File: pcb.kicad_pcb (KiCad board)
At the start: 2 copper layers, 48 parts, among them J1 USB_B_Mini, J2 Conn_ARM_JTAG_SWD_20, J3 Micro_SD_Card_Det1, J4 Conn_02x25_Odd_Even, J5 Conn_02x25_Odd_Even, SW1 SW_RESET, U1 STM32H750VBTx, U2 USBLC6-2P6, U3 TLV1117-33, Y2 25MHz 9uF

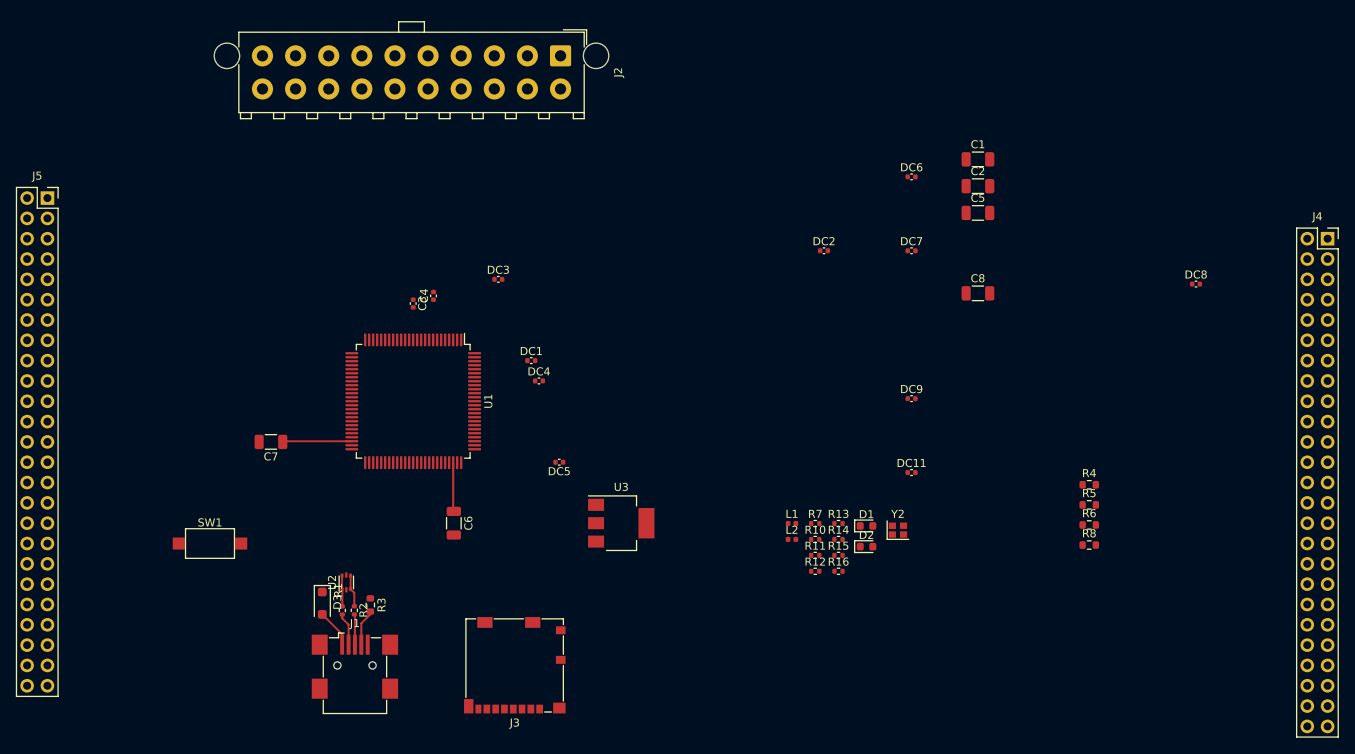
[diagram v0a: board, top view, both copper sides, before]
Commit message: ROUTE: Routing finished, still needs to be re-worked but functionality is in place
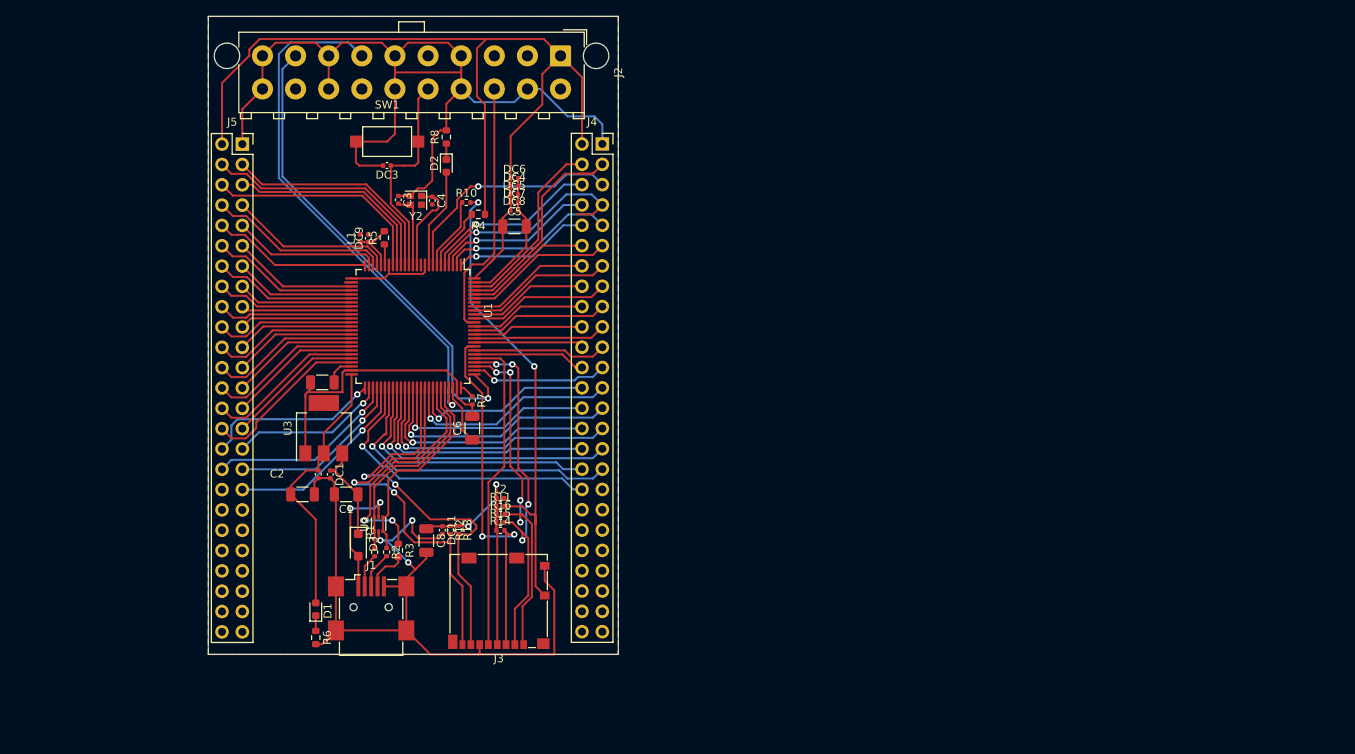
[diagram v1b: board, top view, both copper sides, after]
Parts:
- moved R6 97.7 mm to (74.2, 115.9), turned to -90 degrees
- moved R8 95.2 mm to (90.5, 53.3), turned to 90 degrees
- moved R5 94.2 mm to (82.8, 65.9), turned to 90 degrees
- moved C2 92.8 mm to (72.5, 98.0)
- moved J4 91.4 mm to (110.0, 54.2)
- moved C1 89.4 mm to (78.0, 98.0), turned to 180 degrees
- moved DC8 85.7 mm to (99.0, 62.5)
- moved R4 83.5 mm to (94.5, 63.0), turned to 180 degrees
- moved C8 75.6 mm to (88.0, 103.8), turned to -90 degrees
- moved Y2 73.0 mm to (86.7, 61.2), turned to 180 degrees
- moved D2 70.9 mm to (90.5, 56.9), turned to -90 degrees
- moved DC9 70.8 mm to (80.8, 66.0), turned to 90 degrees
- moved D1 69.6 mm to (74.2, 112.4), turned to 90 degrees
- moved DC2 69.1 mm to (74.5, 95.5), turned to -90 degrees
- moved L1 64.7 mm to (79.8, 66.0), turned to 90 degrees
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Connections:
- J4 pad 1: unconnected-(J4-Pin_1-Pad1) -> Earth
- J4 pad 10: unconnected-(J4-Pin_10-Pad10) -> PE2
- J4 pad 11: unconnected-(J4-Pin_11-Pad11) -> PB8
- J4 pad 12: unconnected-(J4-Pin_12-Pad12) -> PB9
- J4 pad 13: unconnected-(J4-Pin_13-Pad13) -> PB6
- J4 pad 14: unconnected-(J4-Pin_14-Pad14) -> PB7
- J4 pad 15: unconnected-(J4-Pin_15-Pad15) -> PB4
- J4 pad 16: unconnected-(J4-Pin_16-Pad16) -> PB5
- J4 pad 17: unconnected-(J4-Pin_17-Pad17) -> PD6
- J4 pad 18: unconnected-(J4-Pin_18-Pad18) -> PD7
- J4 pad 19: unconnected-(J4-Pin_19-Pad19) -> PD4
- J4 pad 2: unconnected-(J4-Pin_2-Pad2) -> BOOT0
- J4 pad 20: unconnected-(J4-Pin_20-Pad20) -> PD5
- J4 pad 21: unconnected-(J4-Pin_21-Pad21) -> PD1
- J4 pad 22: unconnected-(J4-Pin_22-Pad22) -> PD3
- J4 pad 23: unconnected-(J4-Pin_23-Pad23) -> PA15
- J4 pad 24: unconnected-(J4-Pin_24-Pad24) -> PD0
- J4 pad 25: unconnected-(J4-Pin_25-Pad25) -> PA8
- J4 pad 26: unconnected-(J4-Pin_26-Pad26) -> PA9
- J4 pad 27: unconnected-(J4-Pin_27-Pad27) -> PC6
- J4 pad 28: unconnected-(J4-Pin_28-Pad28) -> PC7
- J4 pad 29: unconnected-(J4-Pin_29-Pad29) -> PD14
- J4 pad 3: unconnected-(J4-Pin_3-Pad3) -> PE0
- J4 pad 30: unconnected-(J4-Pin_30-Pad30) -> PD15
- J4 pad 31: unconnected-(J4-Pin_31-Pad31) -> PD12
- J4 pad 32: unconnected-(J4-Pin_32-Pad32) -> PD13
- J4 pad 33: unconnected-(J4-Pin_33-Pad33) -> PD10
- J4 pad 34: unconnected-(J4-Pin_34-Pad34) -> PD11
- J4 pad 36: unconnected-(J4-Pin_36-Pad36) -> PD9
- J4 pad 4: unconnected-(J4-Pin_4-Pad4) -> PE1
- J4 pad 5: unconnected-(J4-Pin_5-Pad5) -> PC14
- J4 pad 6: unconnected-(J4-Pin_6-Pad6) -> PE6
- J4 pad 7: unconnected-(J4-Pin_7-Pad7) -> PE5
- J4 pad 8: unconnected-(J4-Pin_8-Pad8) -> PE4
- J4 pad 9: unconnected-(J4-Pin_9-Pad9) -> PE3
- J5 pad 1: PE0 -> Earth
- J5 pad 10: PE9 -> PA3
- J5 pad 11: PE10 -> PA4
- J5 pad 12: PE11 -> PA5
- J5 pad 13: PE12 -> PA6
- J5 pad 14: PE13 -> PA7
- J5 pad 15: PE14 -> PC4
- J5 pad 16: PE15 -> PC5
- J5 pad 17: unconnected-(J5-Pin_17-Pad17) -> PB0
- J5 pad 18: unconnected-(J5-Pin_18-Pad18) -> PB1
- J5 pad 19: unconnected-(J5-Pin_19-Pad19) -> PB2
- J5 pad 2: PE1 -> BOOT0
- J5 pad 20: unconnected-(J5-Pin_20-Pad20) -> PE7
- J5 pad 21: unconnected-(J5-Pin_21-Pad21) -> PE8
- J5 pad 22: unconnected-(J5-Pin_22-Pad22) -> PE9
- J5 pad 23: unconnected-(J5-Pin_23-Pad23) -> PE10
- J5 pad 24: unconnected-(J5-Pin_24-Pad24) -> PE11
- J5 pad 25: unconnected-(J5-Pin_25-Pad25) -> PE12
- J5 pad 26: unconnected-(J5-Pin_26-Pad26) -> PE13
- J5 pad 27: unconnected-(J5-Pin_27-Pad27) -> PE14
- J5 pad 28: unconnected-(J5-Pin_28-Pad28) -> PE15
- J5 pad 29: unconnected-(J5-Pin_29-Pad29) -> PB10
- J5 pad 3: PE2 -> PC0
- J5 pad 30: unconnected-(J5-Pin_30-Pad30) -> PB11
- J5 pad 31: unconnected-(J5-Pin_31-Pad31) -> PB13
- J5 pad 32: unconnected-(J5-Pin_32-Pad32) -> PB12
- J5 pad 33: unconnected-(J5-Pin_33-Pad33) -> PB15
- J5 pad 34: unconnected-(J5-Pin_34-Pad34) -> PB14
- J5 pad 35: unconnected-(J5-Pin_35-Pad35) -> PD8
- J5 pad 4: PE3 -> PC1
- J5 pad 5: PE4 -> PC2
- J5 pad 6: PE5 -> PC3
- J5 pad 7: PE6 -> PA0
- J5 pad 8: PE7 -> PA1
- J5 pad 9: PE8 -> PA2
- U1 pad 15: unconnected-(U1-PC0-Pad15) -> PC0
- U1 pad 16: unconnected-(U1-PC1-Pad16) -> PC1
- U1 pad 17: unconnected-(U1-PC2_C-Pad17) -> PC2
- U1 pad 18: unconnected-(U1-PC3_C-Pad18) -> PC3
- U1 pad 22: unconnected-(U1-PA0-Pad22) -> PA0
- U1 pad 23: unconnected-(U1-PA1-Pad23) -> PA1
- U1 pad 24: unconnected-(U1-PA2-Pad24) -> PA2
- U1 pad 25: unconnected-(U1-PA3-Pad25) -> PA3
- U1 pad 28: unconnected-(U1-PA4-Pad28) -> PA4
- U1 pad 29: unconnected-(U1-PA5-Pad29) -> PA5
- U1 pad 30: unconnected-(U1-PA6-Pad30) -> PA6
- U1 pad 31: unconnected-(U1-PA7-Pad31) -> PA7
- U1 pad 32: unconnected-(U1-PC4-Pad32) -> PC4
- U1 pad 33: unconnected-(U1-PC5-Pad33) -> PC5
- U1 pad 34: unconnected-(U1-PB0-Pad34) -> PB0
- U1 pad 35: unconnected-(U1-PB1-Pad35) -> PB1
- U1 pad 36: unconnected-(U1-PB2-Pad36) -> PB2
- U1 pad 46: unconnected-(U1-PB10-Pad46) -> PB10
- U1 pad 47: unconnected-(U1-PB11-Pad47) -> PB11
- U1 pad 51: unconnected-(U1-PB12-Pad51) -> PB12
- U1 pad 52: unconnected-(U1-PB13-Pad52) -> PB13
- U1 pad 53: unconnected-(U1-PB14-Pad53) -> PB14
- U1 pad 54: unconnected-(U1-PB15-Pad54) -> PB15
- U1 pad 55: unconnected-(U1-PD8-Pad55) -> PD8
- U1 pad 56: unconnected-(U1-PD9-Pad56) -> PD9
- U1 pad 57: unconnected-(U1-PD10-Pad57) -> PD10
- U1 pad 58: unconnected-(U1-PD11-Pad58) -> PD11
- U1 pad 59: unconnected-(U1-PD12-Pad59) -> PD12
- U1 pad 60: unconnected-(U1-PD13-Pad60) -> PD13
- U1 pad 61: unconnected-(U1-PD14-Pad61) -> PD14
- U1 pad 62: unconnected-(U1-PD15-Pad62) -> PD15
- U1 pad 63: unconnected-(U1-PC6-Pad63) -> PC6
- U1 pad 64: unconnected-(U1-PC7-Pad64) -> PC7
- U1 pad 67: unconnected-(U1-PA8-Pad67) -> PA8
- U1 pad 68: unconnected-(U1-PA9-Pad68) -> PA9
- U1 pad 77: unconnected-(U1-PA15-Pad77) -> PA15
- U1 pad 8: unconnected-(U1-PC14-Pad8) -> PC14
- U1 pad 81: unconnected-(U1-PD0-Pad81) -> PD0
- U1 pad 82: unconnected-(U1-PD1-Pad82) -> PD1
- U1 pad 84: unconnected-(U1-PD3-Pad84) -> PD3
- U1 pad 85: unconnected-(U1-PD4-Pad85) -> PD4
- U1 pad 86: unconnected-(U1-PD5-Pad86) -> PD5
- U1 pad 87: unconnected-(U1-PD6-Pad87) -> PD6
- U1 pad 88: unconnected-(U1-PD7-Pad88) -> PD7
- U1 pad 90: unconnected-(U1-PB4-Pad90) -> PB4
- U1 pad 91: unconnected-(U1-PB5-Pad91) -> PB5
- U1 pad 92: unconnected-(U1-PB6-Pad92) -> PB6
- U1 pad 93: unconnected-(U1-PB7-Pad93) -> PB7
- U1 pad 95: unconnected-(U1-PB8-Pad95) -> PB8
- U1 pad 96: unconnected-(U1-PB9-Pad96) -> PB9
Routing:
- net Earth: track 0.00 -> 285.5 mm, vias 0 -> 3
- net BOOT0: track 0.00 -> 158.9 mm
- net PA13: track 0.00 -> 67.4 mm, vias 0 -> 1
- net Net-(J3-DET): track 0.00 -> 60.4 mm, vias 0 -> 2
- net PA14: track 0.00 -> 60.0 mm, vias 0 -> 1
- net Net-(J3-DAT0): track 0.00 -> 50.1 mm, vias 0 -> 2
- net Net-(J3-DAT1): track 0.00 -> 49.9 mm, vias 0 -> 2
- net Net-(J3-DAT3/CD): track 0.00 -> 47.1 mm, vias 0 -> 4
- net PD2: track 0.00 -> 45.5 mm, vias 0 -> 2
- net Net-(J3-DAT2): track 0.00 -> 44.8 mm, vias 0 -> 4
- net Net-(J3-CLK): track 0.00 -> 40.1 mm
- net PD10: track 0.00 -> 39.2 mm, vias 0 -> 1
- net PD9: track 0.00 -> 38.2 mm, vias 0 -> 1
- net Net-(J3-VDD): track 0.00 -> 36.8 mm, vias 0 -> 2
- net PD12: track 0.00 -> 35.3 mm, vias 0 -> 1
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- added copper zone on F.Cu, net Earth
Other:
- board outline added: 51.2 x 79.8 mm

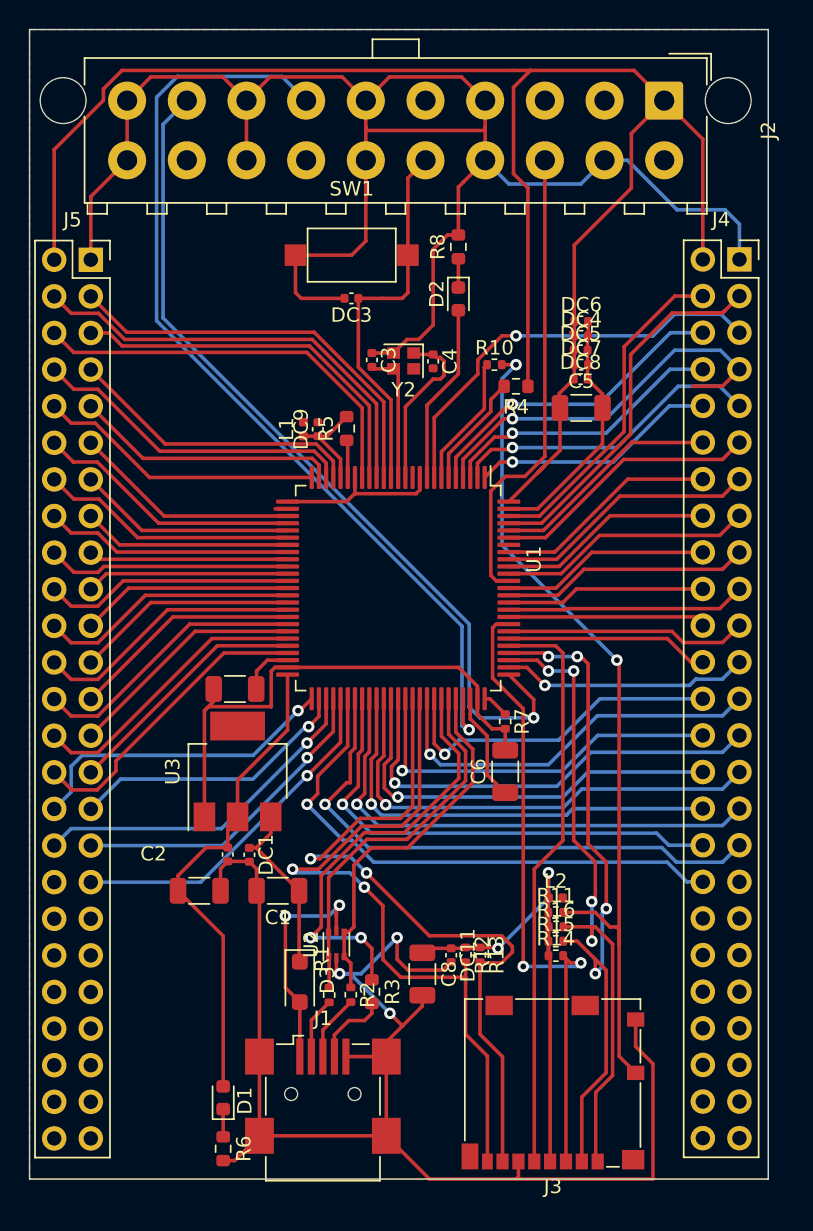
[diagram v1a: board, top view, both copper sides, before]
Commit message: PCB: Routing finished, first version
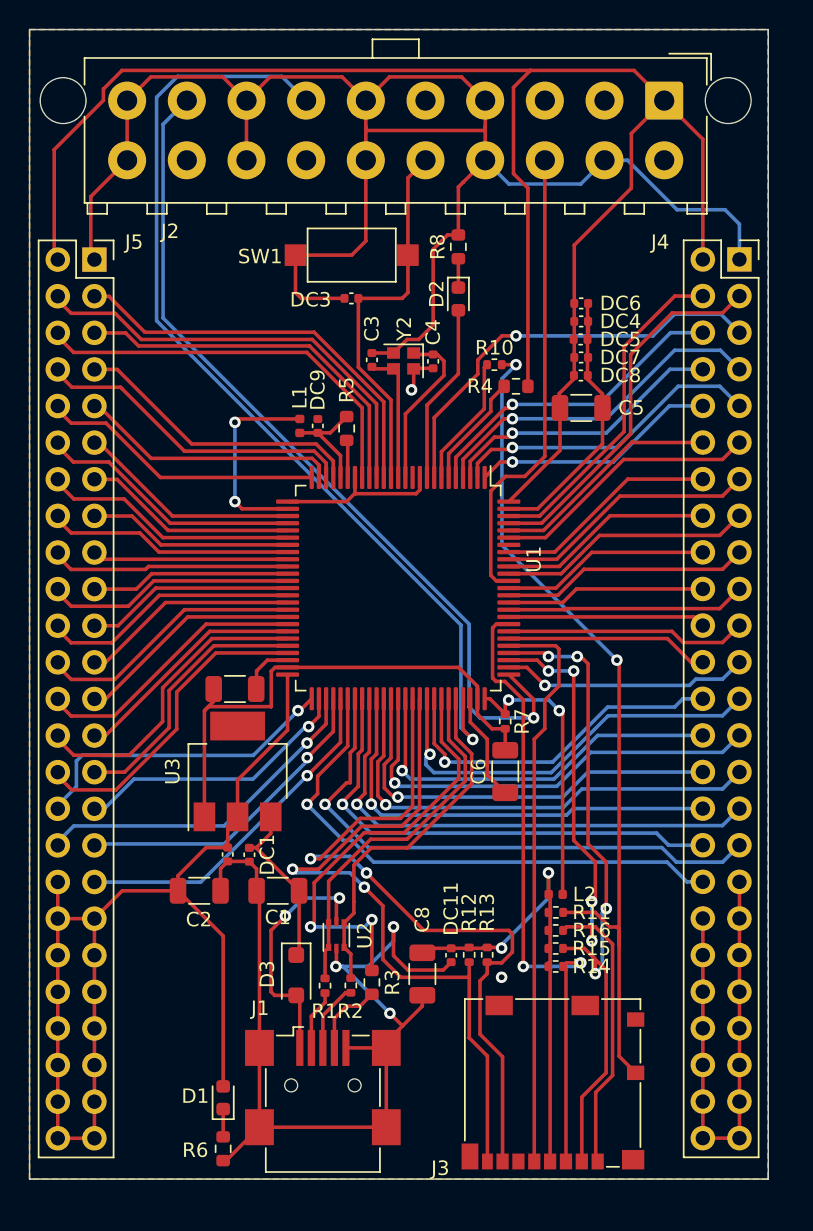
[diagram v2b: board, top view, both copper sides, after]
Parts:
- moved DC6 1.25 mm to (99.0, 57.2)
- moved DC4 1.00 mm to (99.0, 58.5)
- moved R14 0.75 mm to (97.2, 103.2)
- moved DC5 0.75 mm to (99.0, 59.8)
- moved R1 0.71 mm to (81.2, 104.6)
- moved R2 0.64 mm to (83.0, 104.6)
- moved R3 0.64 mm to (84.5, 104.4)
- moved U2 0.64 mm to (82.0, 101.1)
- moved J1 0.60 mm to (81.1, 111.5)
- moved D3 0.53 mm to (79.2, 103.9)
- moved R15 0.50 mm to (97.2, 102.0)
- moved DC7 0.50 mm to (99.0, 61.0)
- moved R13 0.50 mm to (92.5, 102.4)
- moved L1 0.34 mm to (79.5, 65.8)
- moved R16 0.25 mm to (97.2, 100.8)
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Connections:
- J4 pad 35: unconnected-(J4-Pin_35-Pad35) -> Earth
- J4 pad 37: unconnected-(J4-Pin_37-Pad37) -> Earth
- J4 pad 38: unconnected-(J4-Pin_38-Pad38) -> Earth
- J4 pad 39: unconnected-(J4-Pin_39-Pad39) -> Earth
- J4 pad 40: unconnected-(J4-Pin_40-Pad40) -> Earth
- J4 pad 41: unconnected-(J4-Pin_41-Pad41) -> Earth
- J4 pad 42: unconnected-(J4-Pin_42-Pad42) -> Earth
- J4 pad 43: unconnected-(J4-Pin_43-Pad43) -> Earth
- J4 pad 44: unconnected-(J4-Pin_44-Pad44) -> Earth
- J4 pad 45: unconnected-(J4-Pin_45-Pad45) -> Earth
- J4 pad 46: unconnected-(J4-Pin_46-Pad46) -> Earth
- J4 pad 47: unconnected-(J4-Pin_47-Pad47) -> Earth
- J4 pad 48: unconnected-(J4-Pin_48-Pad48) -> Earth
- J4 pad 49: unconnected-(J4-Pin_49-Pad49) -> Earth
- J4 pad 50: unconnected-(J4-Pin_50-Pad50) -> Earth
- J5 pad 36: unconnected-(J5-Pin_36-Pad36) -> BOOT0
- J5 pad 37: unconnected-(J5-Pin_37-Pad37) -> BOOT0
- J5 pad 38: unconnected-(J5-Pin_38-Pad38) -> BOOT0
- J5 pad 39: unconnected-(J5-Pin_39-Pad39) -> BOOT0
- J5 pad 40: unconnected-(J5-Pin_40-Pad40) -> BOOT0
- J5 pad 41: unconnected-(J5-Pin_41-Pad41) -> BOOT0
- J5 pad 42: unconnected-(J5-Pin_42-Pad42) -> BOOT0
- J5 pad 43: unconnected-(J5-Pin_43-Pad43) -> BOOT0
- J5 pad 44: unconnected-(J5-Pin_44-Pad44) -> BOOT0
- J5 pad 45: unconnected-(J5-Pin_45-Pad45) -> BOOT0
- J5 pad 46: unconnected-(J5-Pin_46-Pad46) -> BOOT0
- J5 pad 47: unconnected-(J5-Pin_47-Pad47) -> BOOT0
- J5 pad 48: unconnected-(J5-Pin_48-Pad48) -> BOOT0
- J5 pad 49: unconnected-(J5-Pin_49-Pad49) -> BOOT0
- J5 pad 50: unconnected-(J5-Pin_50-Pad50) -> BOOT0
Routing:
- net BOOT0: track 158.9 -> 233.0 mm, vias 0 -> 4
- net Earth: track 285.5 -> 295.3 mm, vias 3 -> 5
- net PE5: track 28.2 -> 24.1 mm
- net Net-(J3-VDD): track 36.8 -> 33.2 mm
- net PE0: track 27.8 -> 25.8 mm
- net PE15: track 20.0 -> 21.5 mm
- net PA8: track 27.6 -> 28.9 mm
- net PA13: track 67.4 -> 68.7 mm
- net PB10: track 17.3 -> 18.5 mm
- net PB11: track 21.0 -> 22.1 mm
- net +5V: track 12.7 -> 11.8 mm
- net Net-(D3-A): track 16.4 -> 17.3 mm
- net Net-(U1-PA12): track 26.1 -> 25.2 mm
- net PA9: track 23.7 -> 24.4 mm
- net Net-(U1-PA11): track 26.1 -> 25.4 mm
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- added copper zone on B.Cu, net Earth

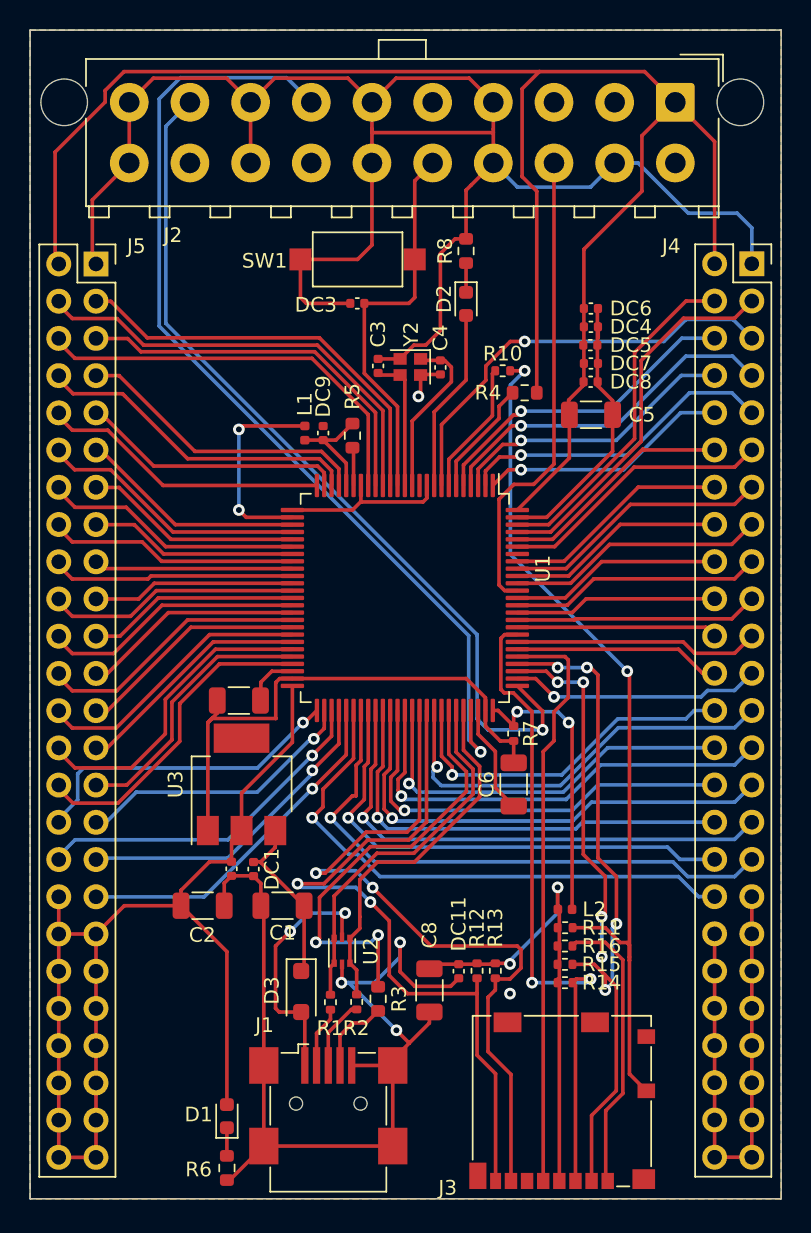
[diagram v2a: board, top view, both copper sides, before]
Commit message: PCB: Updated footprint of JTAG connector
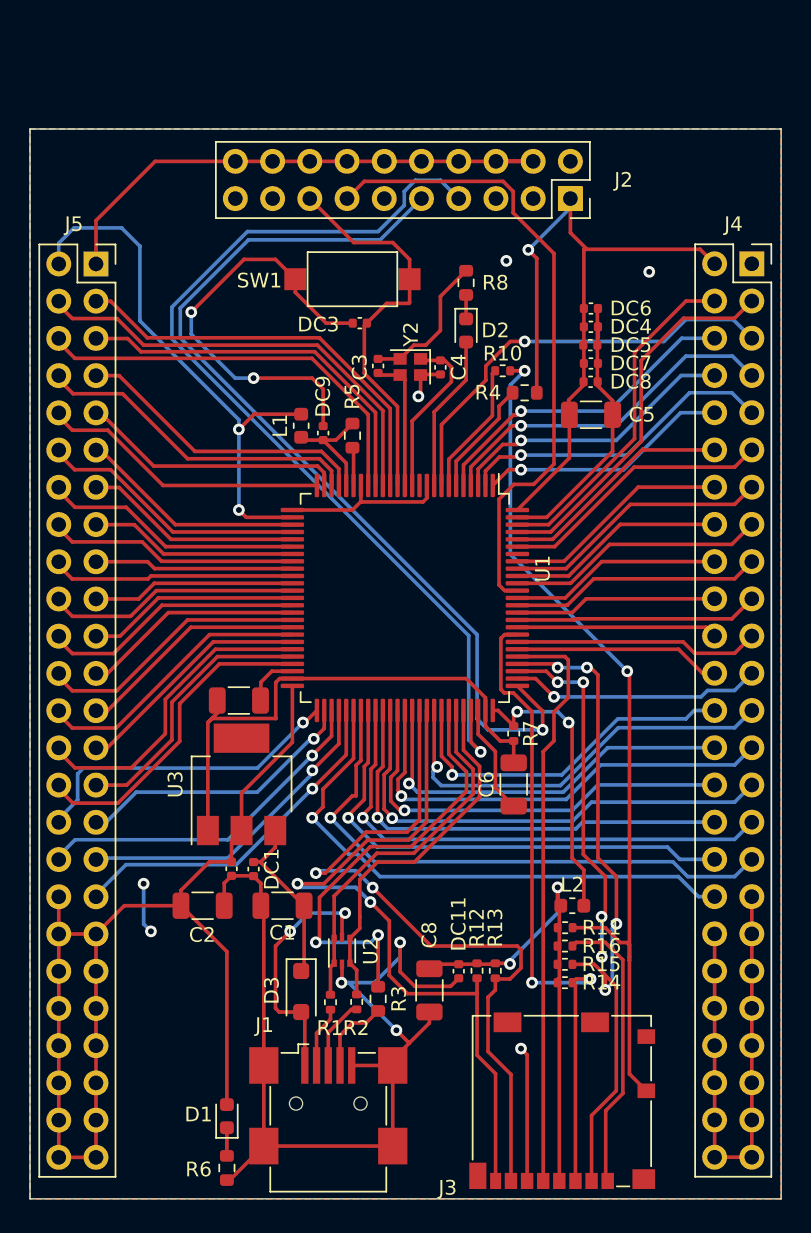
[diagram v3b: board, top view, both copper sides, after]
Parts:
- J2: footprint Connector_TE-Connectivity:TE_MATE-N-LOK_1-794070-x_2x10_P4.14mm_Vertical -> Connector_PinSocket_2.54mm:PinSocket_2x10_P2.54mm_Vertical
- L1, L2: footprint Inductor_SMD:L_0402_1005Metric -> Inductor_SMD:L_0603_1608Metric
- Y2: value 25MHz 9uF -> 25MHz 9pF
- moved J2 9.72 mm to (97.6, 49.8)
- moved R8 2.17 mm to (90.5, 55.5)
- moved D2 1.81 mm to (90.5, 58.8)
- moved SW1 1.39 mm to (82.8, 55.2)
- moved DC3 1.36 mm to (83.2, 58.2)
- moved L1 0.56 mm to (79.2, 65.2)
- moved L2 0.56 mm to (97.8, 98.0)
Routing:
- net BOOT0: track 233.0 -> 183.2 mm, vias 4 -> 5
- net Earth: track 295.3 -> 263.8 mm, vias 5 -> 11
- net PB3: track 32.5 -> 43.9 mm
- net PA14: track 60.0 -> 64.5 mm
- net PA13: track 68.7 -> 66.4 mm
- net Net-(D2-A): track 12.5 -> 10.7 mm
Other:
- board size 51.2 x 79.8 mm -> 51.2 x 73 mm
- board text added: "10-Year Anniversary v1.2"

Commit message: BOM: Added bill of material
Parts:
- moved J2 1.25 mm to (97.6, 51.0)
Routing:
- net Earth: track 263.8 -> 242.0 mm
- net BOOT0: track 183.2 -> 198.4 mm
- net PA13: track 66.4 -> 70.6 mm
- net PA14: track 64.5 -> 68.0 mm
- net RESET: track 27.1 -> 28.6 mm
- net PB3: track 43.9 -> 43.0 mm
